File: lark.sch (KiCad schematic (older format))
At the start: 38 parts

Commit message: Remove orphan GPS PPS signal
Remove orphan.
Give up on GPS PPS feed. Not enough pins.
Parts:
- removed R?: 470, symbol R
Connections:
- net labels removed: GPS_PPS
- wire segments 145 -> 144
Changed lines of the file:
@@
 Wire Wire Line
 	10150 5750 9900 5750
-Text GLabel 7100 3650 2    47   Input ~ 0
-GPS_PPS
-$Comp
-L R R?
-U 1 1 5A67F987
-P 6900 3650
-F 0 "R?" H 6930 3670 50  0000 L CNN
-F 1 "470" H 6930 3610 50  0000 L CNN
-F 2 "" H 6900 3650 50  0000 C CNN
-F 3 "" H 6900 3650 50  0000 C CNN
-	1    6900 3650
-	0    1    1    0
-$EndComp
 Wire Wire Line
 	6700 1700 7050 1700
@@
 Wire Wire Line
 	2150 4100 2650 4100
-Wire Wire Line
-	7000 3650 7100 3650
 $Comp
 L R R?

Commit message: Finalize schematics and component selection
Remove SD interface
Rework power supplies
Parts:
- removed J?: TF_1, symbol TF_1
- C1, C2, C3, C4, C6, C7: renamed from C?; value C -> 10n; footprint (none) -> Capacitors_SMD:C_0805_HandSoldering; PartNo (none) -> 08055C103KAT2A
- C10, C8: renamed from C?; value C -> 100n; footprint (none) -> Capacitors_SMD:C_0805_HandSoldering; PartNo (none) -> 08055C104KAT2A
- C5: renamed from C?; value 1nF -> 10n; footprint (none) -> Capacitors_SMD:C_0805_HandSoldering; PartNo (none) -> 08055C103KAT2A
- C9: renamed from C?; value CP -> 22u; footprint (none) -> Capacitors_SMD:C_1206_HandSoldering; symbol CP -> C; PartNo (none) -> CL31A226KPHNNNE
- D1: renamed from D?; footprint (none) -> LEDs:LED_1206; PartNo (none) -> LTST-C150CKT
- J1, J2: renamed from J?; footprint (none) -> Socket_Strips:Socket_Strip_Straight_1x06_Pitch2.54mm
- J3: renamed from J?; footprint (none) -> Socket_Strips:Socket_Strip_Straight_1x02_Pitch2.54mm
- R1: renamed from R?; value R -> 330R; footprint (none) -> Resistors_SMD:R_0805_HandSoldering; PartNo (none) -> RC0805FR-07330RL
- R10: renamed from R?; value 0 -> 0R; footprint (none) -> Resistors_SMD:R_0805_HandSoldering; PartNo (none) -> AC0805JR-070RL
- R11: renamed from R?; value 100k -> DNP; footprint (none) -> Resistors_SMD:R_0805_HandSoldering
- R12: renamed from R?; footprint (none) -> Resistors_SMD:R_0805_HandSoldering; PartNo (none) -> RC0805FR-07100KL
- R13: renamed from R?; value R -> 0R; footprint (none) -> Resistors_SMD:R_0805_HandSoldering; PartNo (none) -> AC0805JR-070RL
- R14: renamed from R?; value R -> 390k; footprint (none) -> Resistors_SMD:R_0805_HandSoldering; PartNo (none) -> RT0805BRD07390KL
- R15: renamed from R?; value R -> 100k; footprint (none) -> Resistors_SMD:R_0805_HandSoldering; PartNo (none) -> RT0805BRE07100KL
- R2, R3, R4, R5, R6, R7, R9: renamed from R?; value R -> 100k; footprint (none) -> Resistors_SMD:R_0805_HandSoldering; PartNo (none) -> RC0805FR-07100KL
- R8: renamed from R?; value 470 -> 470R; footprint (none) -> Resistors_SMD:R_0805_HandSoldering; PartNo (none) -> RC0805FR-07470RL
- SW1, SW5: renamed from SW?; footprint (none) -> Socket_Strips:Socket_Strip_Straight_1x02_Pitch2.54mm
- SW2, SW3, SW4: renamed from SW?; footprint (none) -> Buttons_Switches_THT:SW_Tactile_SKHH_Angled; PartNo (none) -> 2-1825027-0
- U1: renamed from U?; footprint ESP32-footprints-Lib:ESP32-WROOM -> components:ESP32-WROOM
- U2: renamed from U?; footprint (none) -> Housings_DFN_QFN:QFN-16-1EP_3x3mm_Pitch0.5mm; PartNo (none) -> MAX98357AETE+TCT-ND
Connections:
- net labels removed: MMC_IO2, MMC_IO4
- wire segments 144 -> 131
- no-connect marks 9 -> 10

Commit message: Rework the schematic from scratch
Rework basic ESP32 pin assignment
Rework power supply
Rework interface
Rework sound generation - remove I2C codec, use internal DAC
Add D-class amplifier
Add Serial lines
Add USB charger
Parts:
- removed C1, C2, C3, C4, C5, C6, C7: 10n, Capacitors_SMD:C_0805_HandSoldering, symbol C
- removed C10, C8: 100n, Capacitors_SMD:C_0805_HandSoldering, symbol C
- removed C9: 22u, Capacitors_SMD:C_1206_HandSoldering, symbol C
- removed D1: LED, LEDs:LED_1206, symbol LED
- removed J1, J2: Conn_01x06, Socket_Strips:Socket_Strip_Straight_1x06_Pitch2.54mm, symbol Conn_01x06
- removed J3: Conn_01x02, Socket_Strips:Socket_Strip_Straight_1x02_Pitch2.54mm, symbol Conn_01x02
- removed R1: 330R, Resistors_SMD:R_0805_HandSoldering, symbol R
- removed R10, R13: 0R, Resistors_SMD:R_0805_HandSoldering, symbol R
- removed R11: DNP, Resistors_SMD:R_0805_HandSoldering, symbol R
- removed R12, R15, R2, R3, R4, R5, R6, R7, R9: 100k, Resistors_SMD:R_0805_HandSoldering, symbol R
- removed R14: 390k, Resistors_SMD:R_0805_HandSoldering, symbol R
- removed R8: 470R, Resistors_SMD:R_0805_HandSoldering, symbol R
- removed SW1, SW5: SW_SPST, Socket_Strips:Socket_Strip_Straight_1x02_Pitch2.54mm, symbol SW_SPST
- removed SW2, SW3, SW4: SW_Push, Buttons_Switches_THT:SW_Tactile_SKHH_Angled, symbol SW_Push
- removed U1: ESP32-WROOM, components:ESP32-WROOM, symbol ESP32-WROOM
- removed U2: MAX98357, Housings_DFN_QFN:QFN-16-1EP_3x3mm_Pitch0.5mm, symbol MAX98357
- added C? (x7): 100n, symbol Device:C
- added D? (x2): LED, symbol Device:LED
- added J?: Conn_01x06, symbol Connector_Generic:Conn_01x06
- added J?: Conn_01x07, symbol Connector_Generic:Conn_01x07
- added MOD1: ESP32-WROOM-32, digikey-footprints:ESP32-WROOM-32D, symbol dk_RF-Transceiver-Modules:ESP32-WROOM-32
- added R? (x16): 10k, symbol Device:R
- added R? (x4): NC, symbol Device:R
- added R?: 100k, symbol Device:R
- added R?: 390k, symbol Device:R
- added R? (x3): 470R, symbol Device:R
- added R?: 0R, symbol Device:R
- added SW?: SW_DPST_x2, symbol Switch:SW_DPST_x2
- added SW? (x3): SW_Push, symbol Switch:SW_Push
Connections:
- net labels added: BUT_DOWN, BUT_ENTR, BUT_UP, I2C_SCK, LED1, LED2, SND_L, SND_R, SPICLK, SPICS0, SPICS1, SPICS2, SPID, SPIQ, SW_VARIO, U0RXD, U0TXD, U1CTS, U1RTS, U1RXD, U1TXD, U2RXD, U2TXD, VDD
- net labels removed: +12V, +3.3V, ENTR, I2C_SCL, I2S_BCLK, I2S_DAT, I2S_LRCLK, INDLED, MTCK, MTDI, MTDO, MTMS, RXD0, SPI_CS0, SPI_CS1, SPI_MISO, SPI_MOSI, SPI_SCLK, STF/VARIO, TAMPER, TDX0, VOLN, VOLP
- wire segments 131 -> 191
- no-connect marks 10 -> 6

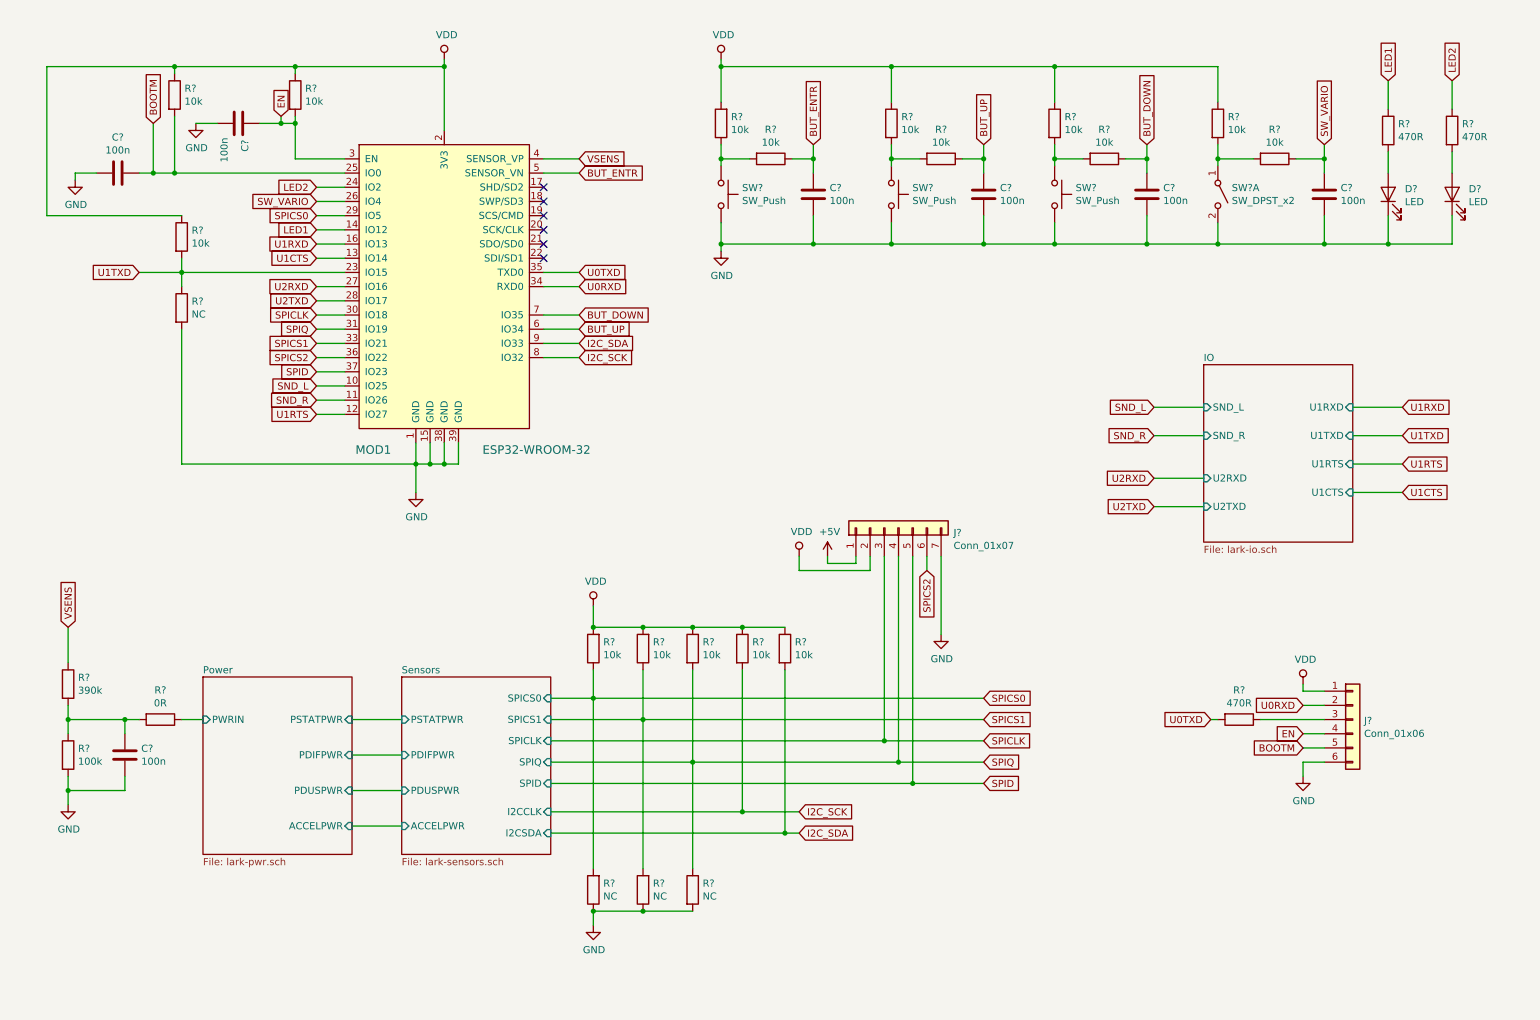
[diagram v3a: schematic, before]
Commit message: Finalize schematic
Finish part selection

Pending issues: IMU, switches & LEDs, mechanical parts and housing
selection.
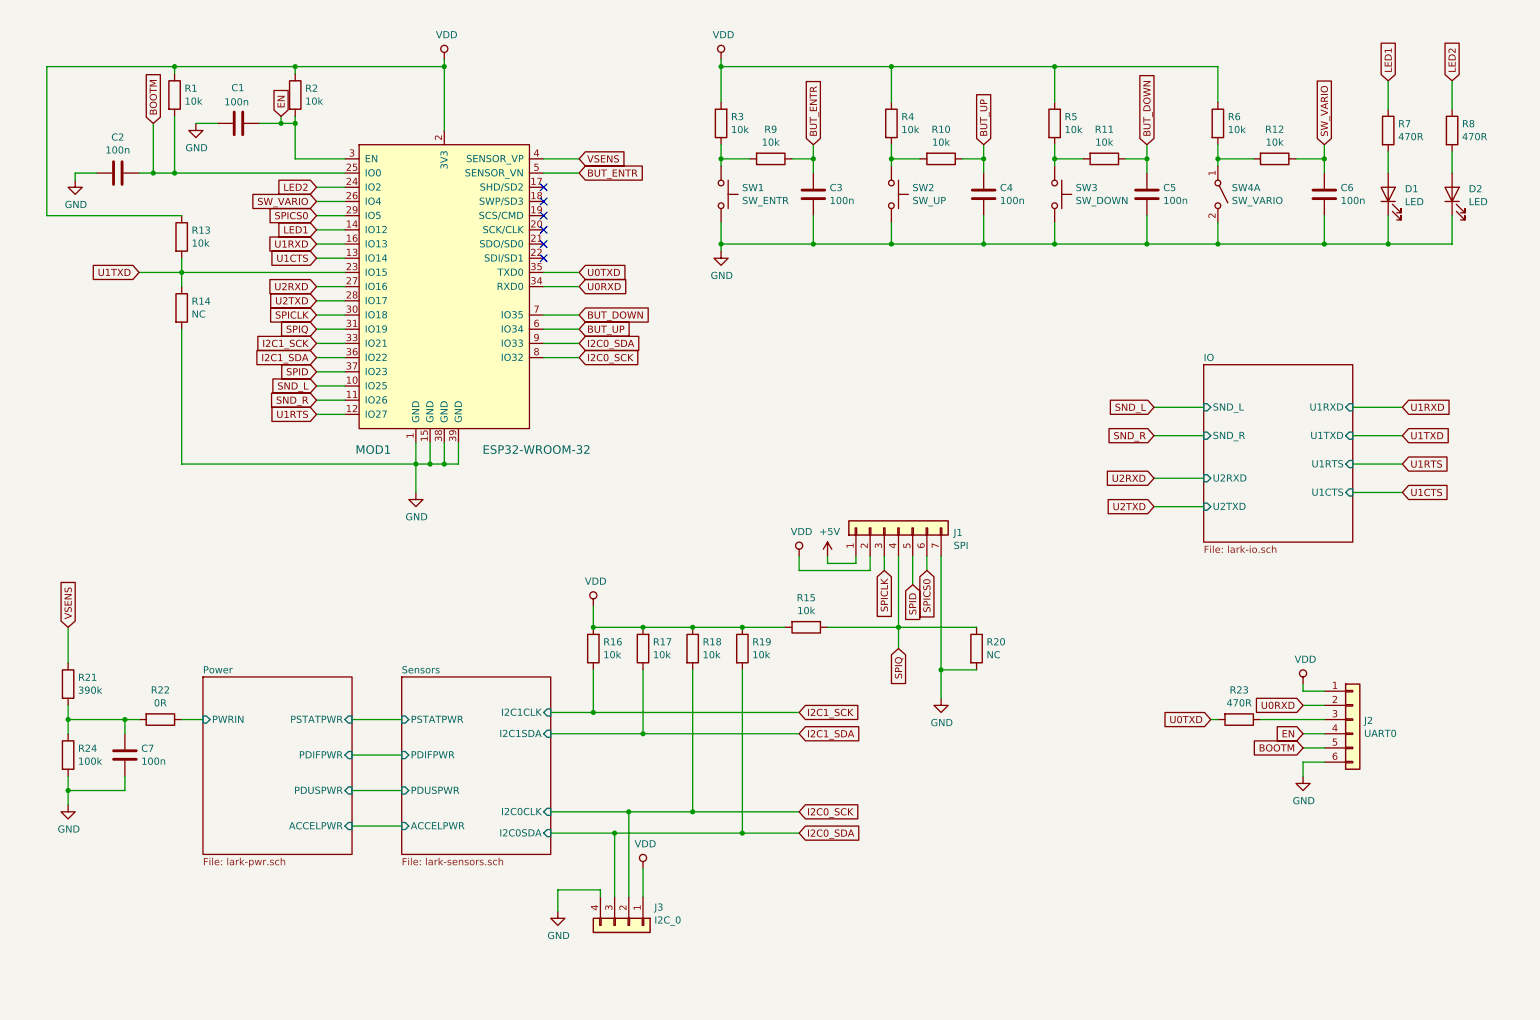
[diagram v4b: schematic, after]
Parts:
- removed R? (x2): NC, symbol Device:R
- removed R?: 10k, symbol Device:R
- added J3: I2C_0, Connector_PinHeader_2.54mm:PinHeader_1x04_P2.54mm_Vertical, symbol Connector_Generic:Conn_01x04
- added R15: 10k, Resistor_SMD:R_0805_2012Metric_Pad1.15x1.40mm_HandSolder, symbol Device:R
- C1, C2, C3, C4, C5, C6: renamed from C?; footprint (none) -> Capacitor_SMD:C_0805_2012Metric_Pad1.15x1.40mm_HandSolder; MPN (none) -> 885012207128
- C7: renamed from C?; footprint (none) -> Capacitor_SMD:C_0805_2012Metric_Pad1.15x1.40mm_HandSolder
- D1: renamed from D?; footprint (none) -> LED_SMD:LED_1206_3216Metric_Pad1.42x1.75mm_HandSolder; MPN (none) -> LTST-C150GKT
- D2: renamed from D?; footprint (none) -> LED_SMD:LED_1206_3216Metric_Pad1.42x1.75mm_HandSolder; MPN (none) -> LTST-C150CKT
- J1: renamed from J?; value Conn_01x07 -> SPI; footprint (none) -> Connector_PinHeader_2.54mm:PinHeader_1x07_P2.54mm_Vertical
- J2: renamed from J?; value Conn_01x06 -> UART0; footprint (none) -> Connector_PinHeader_2.54mm:PinHeader_1x06_P2.54mm_Vertical
- R1, R10, R11, R12, R13, R16, R17, R18, R19, R2, R3, R4, R5, R6, R9: renamed from R?; footprint (none) -> Resistor_SMD:R_0805_2012Metric_Pad1.15x1.40mm_HandSolder; MPN (none) -> RC0805FR-0710KL
- R14, R20: renamed from R?; footprint (none) -> Resistor_SMD:R_0805_2012Metric_Pad1.15x1.40mm_HandSolder
- R21: renamed from R?; footprint (none) -> Resistor_SMD:R_0805_2012Metric_Pad1.15x1.40mm_HandSolder; MPN (none) -> RT0805BRD07390KL
- R22: renamed from R?; footprint (none) -> Resistor_SMD:R_0805_2012Metric_Pad1.15x1.40mm_HandSolder; MPN (none) -> RC0805JR-070RL
- R23, R7, R8: renamed from R?; footprint (none) -> Resistor_SMD:R_0805_2012Metric_Pad1.15x1.40mm_HandSolder; MPN (none) -> RC0805FR-07470RL
- R24: renamed from R?; footprint (none) -> Resistor_SMD:R_0805_2012Metric_Pad1.15x1.40mm_HandSolder; MPN (none) -> RT0805BRD07100KL
- SW1: renamed from SW?; value SW_Push -> SW_ENTR; footprint (none) -> Button_Switch_THT:SW_Tactile_SPST_Angled_PTS645Vx83-2LFS; MPN (none) -> PTS645VH83-2 LFS
- SW2: renamed from SW?; value SW_Push -> SW_UP; footprint (none) -> Button_Switch_THT:SW_Tactile_SPST_Angled_PTS645Vx83-2LFS; MPN (none) -> PTS645VH83-2 LFS
- SW3: renamed from SW?; value SW_Push -> SW_DOWN; footprint (none) -> Button_Switch_THT:SW_Tactile_SPST_Angled_PTS645Vx83-2LFS; MPN (none) -> PTS645VH83-2 LFS
- SW4: renamed from SW?; value SW_DPST_x2 -> SW_VARIO; footprint (none) -> TerminalBlock_Phoenix:TerminalBlock_Phoenix_PT-1,5-2-3.5-H_1x02_P3.50mm_Horizontal; MPN (none) -> 277-1721-ND
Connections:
- net GND: now also J3.4 (Pin_4)
- net SPICS0: now also J1.6 (Pin_6); no longer R16.1
- net SPIQ: now also R15.1; no longer R18.2
- net VDD: now also J3.1 (Pin_1), R15.2
- net I2C_SCK renamed I2C0_SCK
- net I2C0_SCK: now also R18.2, J3.2 (Pin_2); no longer R19.2
- net I2C_SDA renamed I2C0_SDA
- net I2C0_SDA: now also R19.2, J3.3 (Pin_3)
- net SPICS1 renamed I2C1_SCK
- net I2C1_SCK: now also R16.1; no longer R17.1
- net SPICS2 renamed I2C1_SDA
- net I2C1_SDA: now also R17.1; no longer J1.6 (Pin_6)
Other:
- moved on the sheet: R20

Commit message: Fill in all remaining PNs in the schematics
Finish the part selection, let's hope for least possible number of mistakes.
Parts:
- C7: MPN (none) -> 885012207128
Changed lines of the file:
@@
 F 2 "Capacitor_SMD:C_0805_2012Metric_Pad1.15x1.40mm_HandSolder" H 1338 5700 50  0001 C CNN
 F 3 "~" H 1300 5850 50  0001 C CNN
+F 4 "885012207128" H 0   0   50  0001 C CNN "MPN"
 	1    1300 5850
 	1    0    0    -1

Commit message: Intermediate status while arranging compontents.
Manually grouped components into smaller islands.

Some parts were changed:
* U1: SOT-23-3 LDO should be sufficient
* CP_Elec: Use 10x10 size
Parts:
- MOD1: symbol dk_RF-Transceiver-Modules:ESP32-WROOM-32 -> lark-rescue:ESP32-WROOM-32-dk_RF-Transceiver-Modules
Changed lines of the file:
@@
 $EndDescr
 $Comp
-L dk_RF-Transceiver-Modules:ESP32-WROOM-32 MOD1
+L lark-rescue:ESP32-WROOM-32-dk_RF-Transceiver-Modules MOD1
 U 1 1 5C429E20
 P 3350 1550

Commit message: continue layout work, WIP
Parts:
- C1, C2, C3, C4, C5, C6, C7: symbol Device:C -> lark-rescue:C-Device
- D1, D2: symbol Device:LED -> lark-rescue:LED-Device
- J1: symbol Connector_Generic:Conn_01x07 -> lark-rescue:Conn_01x07-Connector_Generic
- J2: symbol Connector_Generic:Conn_01x06 -> lark-rescue:Conn_01x06-Connector_Generic
- J3: symbol Connector_Generic:Conn_01x04 -> lark-rescue:Conn_01x04-Connector_Generic
- R1, R10, R11, R12, R13, R14, R15, R16, R17, R18, R19, R2, R20, R21, R22, R23, R24, R3, R4, R5, R6, R7, R8, R9: symbol Device:R -> lark-rescue:R-Device
- SW1, SW2, SW3: symbol Switch:SW_Push -> lark-rescue:SW_Push-Switch
- SW4: symbol Switch:SW_DPST_x2 -> lark-rescue:SW_DPST_x2-Switch
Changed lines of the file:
@@
 $EndComp
 $Comp
-L power:GND #PWR06
+L lark-rescue:GND-power #PWR06
 U 1 1 5C429F76
 P 3350 4000
@@
 $EndComp
 $Comp
-L power:VDD #PWR01
+L lark-rescue:VDD-power #PWR01
 U 1 1 5C42AE71
 P 3550 950
@@
 $EndComp
 $Comp
-L Device:C C1
+L lark-rescue:C-Device C1
 U 1 1 5C42AF26
 P 2100 1400
@@
 $EndSheet
 $Comp
-L power:GND #PWR03
+L lark-rescue:GND-power #PWR03
 U 1 1 5C42BE5E
 P 1800 1400
@@
 EN
 $Comp
-L Device:R R1
+L lark-rescue:R-Device R1
 U 1 1 5C4FD11A
 P 1650 1200
@@
 Connection ~ 1650 1750
 $Comp
-L Device:C C2
+L lark-rescue:C-Device C2
 U 1 1 5C5007D1
 P 1250 1750
@@
 $EndComp
 $Comp
-L power:GND #PWR04
+L lark-rescue:GND-power #PWR04
 U 1 1 5C500861
 P 950 1800
@@
 Connection ~ 2500 1000
 $Comp
-L Device:R R2
+L lark-rescue:R-Device R2
 U 1 1 5C501FFD
 P 2500 1200
@@
 U1TXD
 $Comp
-L Device:R R13
+L lark-rescue:R-Device R13
 U 1 1 5C505E70
 P 1700 2200
@@
 $EndComp
 $Comp
-L Device:R R14
+L lark-rescue:R-Device R14
 U 1 1 5C505ED8
 P 1700 2700
@@
 I2C1_SDA
 $Comp
-L Device:R R16
+L lark-rescue:R-Device R16
 U 1 1 5C5EB518
 P 4600 5100
@@
 $EndComp
 $Comp
-L Device:R R17
+L lark-rescue:R-Device R17
 U 1 1 5C5EB606
 P 4950 5100
@@
 $EndComp
 $Comp
-L power:VDD #PWR09
+L lark-rescue:VDD-power #PWR09
 U 1 1 5C5EB6C8
 P 4600 4800
@@
 SPID
 $Comp
-L Device:R R24
+L lark-rescue:R-Device R24
 U 1 1 5C607182
 P 900 5850
@@
 $EndComp
 $Comp
-L Device:C C7
+L lark-rescue:C-Device C7
 U 1 1 5C607206
 P 1300 5850
@@
 $EndComp
 $Comp
-L power:GND #PWR013
+L lark-rescue:GND-power #PWR013
 U 1 1 5C60729B
 P 900 6200
@@
 	900  5700 900  5600
 $Comp
-L Device:R R21
+L lark-rescue:R-Device R21
 U 1 1 5C61497E
 P 900 5350
@@
 	4250 1650 4500 1650
 $Comp
-L Device:R R18
+L lark-rescue:R-Device R18
 U 1 1 5C63E997
 P 5300 5100
@@
 I2C0_SDA
 $Comp
-L Device:R R20
+L lark-rescue:R-Device R20
 U 1 1 5C65297A
 P 7300 5100
@@
 $EndComp
 $Comp
-L Device:R R19
+L lark-rescue:R-Device R19
 U 1 1 5C6529D9
 P 5650 5100
@@
 $EndSheet
 $Comp
-L power:VDD #PWR010
+L lark-rescue:VDD-power #PWR010
 U 1 1 5C54DF15
 P 9600 5350
@@
 $EndComp
 $Comp
-L power:GND #PWR012
+L lark-rescue:GND-power #PWR012
 U 1 1 5C54DFCE
 P 9600 6000
@@
 	9600 5400 9750 5400
 $Comp
-L Connector_Generic:Conn_01x06 J2
+L lark-rescue:Conn_01x06-Connector_Generic J2
 U 1 1 5C55381F
 P 9950 5600
@@
 LED2
 $Comp
-L Switch:SW_DPST_x2 SW4
+L lark-rescue:SW_DPST_x2-Switch SW4
 U 1 1 5C562635
 P 9000 1900
@@
 $EndComp
 $Comp
-L Switch:SW_Push SW1
+L lark-rescue:SW_Push-Switch SW1
 U 1 1 5C562BE8
 P 5500 1900
@@
 $EndComp
 $Comp
-L Switch:SW_Push SW2
+L lark-rescue:SW_Push-Switch SW2
 U 1 1 5C562CC3
 P 6700 1900
@@
 $EndComp
 $Comp
-L Device:R R3
+L lark-rescue:R-Device R3
 U 1 1 5C562FAC
 P 5500 1400
@@
 $EndComp
 $Comp
-L Switch:SW_Push SW3
+L lark-rescue:SW_Push-Switch SW3
 U 1 1 5C59ED05
 P 7850 1900
@@
 $EndComp
 $Comp
-L Device:R R9
+L lark-rescue:R-Device R9
 U 1 1 5C5A20AC
 P 5850 1650
@@
 $EndComp
 $Comp
-L Device:C C3
+L lark-rescue:C-Device C3
 U 1 1 5C5A2192
 P 6150 1900
@@
 $EndComp
 $Comp
-L power:VDD #PWR02
+L lark-rescue:VDD-power #PWR02
 U 1 1 5C5A546A
 P 5500 950
@@
 $EndComp
 $Comp
-L power:GND #PWR05
+L lark-rescue:GND-power #PWR05
 U 1 1 5C5A551C
 P 5500 2300
@@
 	5500 2250 5500 2300
 $Comp
-L Device:R R4
+L lark-rescue:R-Device R4
 U 1 1 5C5C4642
 P 6700 1400
@@
 $EndComp
 $Comp
-L Device:R R10
+L lark-rescue:R-Device R10
 U 1 1 5C5C47D3
 P 7050 1650
@@
 $EndComp
 $Comp
-L Device:C C4
+L lark-rescue:C-Device C4
 U 1 1 5C5C4913
 P 7350 1900
@@
 Connection ~ 7350 1650
 $Comp
-L Device:R R5
+L lark-rescue:R-Device R5
 U 1 1 5C5EF273
 P 7850 1400
@@
 $EndComp
 $Comp
-L Device:R R11
+L lark-rescue:R-Device R11
 U 1 1 5C5EF3D3
 P 8200 1650
@@
 $EndComp
 $Comp
-L Device:C C5
+L lark-rescue:C-Device C5
 U 1 1 5C5EF4B7
 P 8500 1900
@@
 Connection ~ 6700 1000
 $Comp
-L Device:R R6
+L lark-rescue:R-Device R6
 U 1 1 5C60D434
 P 9000 1400
@@
 $EndComp
 $Comp
-L Device:R R12
+L lark-rescue:R-Device R12
 U 1 1 5C60D552
 P 9400 1650
@@
 $EndComp
 $Comp
-L Device:C C6
+L lark-rescue:C-Device C6
 U 1 1 5C60D6AA
 P 9750 1900
@@
 Connection ~ 9750 1650
 $Comp
-L Device:LED D1
+L lark-rescue:LED-Device D1
 U 1 1 5C634D2B
 P 10200 1900
@@
 $EndComp
 $Comp
-L Device:LED D2
+L lark-rescue:LED-Device D2
 U 1 1 5C63A623
 P 10650 1900
@@
 Connection ~ 10200 2250
 $Comp
-L Device:R R7
+L lark-rescue:R-Device R7
 U 1 1 5C64A79A
 P 10200 1450
@@
 $EndComp
 $Comp
-L Device:R R8
+L lark-rescue:R-Device R8
 U 1 1 5C64A8A6
 P 10650 1450
@@
 	10200 1750 10200 1600
 $Comp
-L Device:R R23
+L lark-rescue:R-Device R23
 U 1 1 5C67286C
 P 9150 5600
@@
 	1300 5600 1300 5700
 $Comp
-L Device:R R22
+L lark-rescue:R-Device R22
 U 1 1 5C6C8719
 P 1550 5600
@@
 	1700 5600 1850 5600
 $Comp
-L Connector_Generic:Conn_01x07 J1
+L lark-rescue:Conn_01x07-Connector_Generic J1
 U 1 1 5C6997BC
 P 6750 4250
@@
 $EndComp
 $Comp
-L power:GND #PWR011
+L lark-rescue:GND-power #PWR011
 U 1 1 5C6A0268
 P 7050 5450
@@
 $EndComp
 $Comp
-L power:VDD #PWR07
+L lark-rescue:VDD-power #PWR07
 U 1 1 5C6A0347
 P 6050 4450
@@
 $EndComp
 $Comp
-L power:+5V #PWR08
+L lark-rescue:+5V-power #PWR08
 U 1 1 5C6A04D5
 P 6250 4450
@@
 	7050 5250 7050 5450
 $Comp
-L Device:R R15
+L lark-rescue:R-Device R15
 U 1 1 5C7133A8
 P 6100 4950
@@
 $EndComp
 $Comp
-L Connector_Generic:Conn_01x04 J3
+L lark-rescue:Conn_01x04-Connector_Generic J3
 U 1 1 5C71487D
 P 4850 7050
@@
 $EndComp
 $Comp
-L power:VDD #PWR014
+L lark-rescue:VDD-power #PWR014
 U 1 1 5C72D89B
 P 4950 6650
@@
 $EndComp
 $Comp
-L power:GND #PWR015
+L lark-rescue:GND-power #PWR015
 U 1 1 5C72D962
 P 4350 6950
